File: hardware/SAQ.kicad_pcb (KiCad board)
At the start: 2 copper layers, 61 x 43.2 mm, 40 parts, among them J1 Sens, J2 9V, J3 AudioJack2_Ground_Switch, J4 SP, Q1 2N3904, SW1 SW_SPDT, U1 LM555, U2 LM386

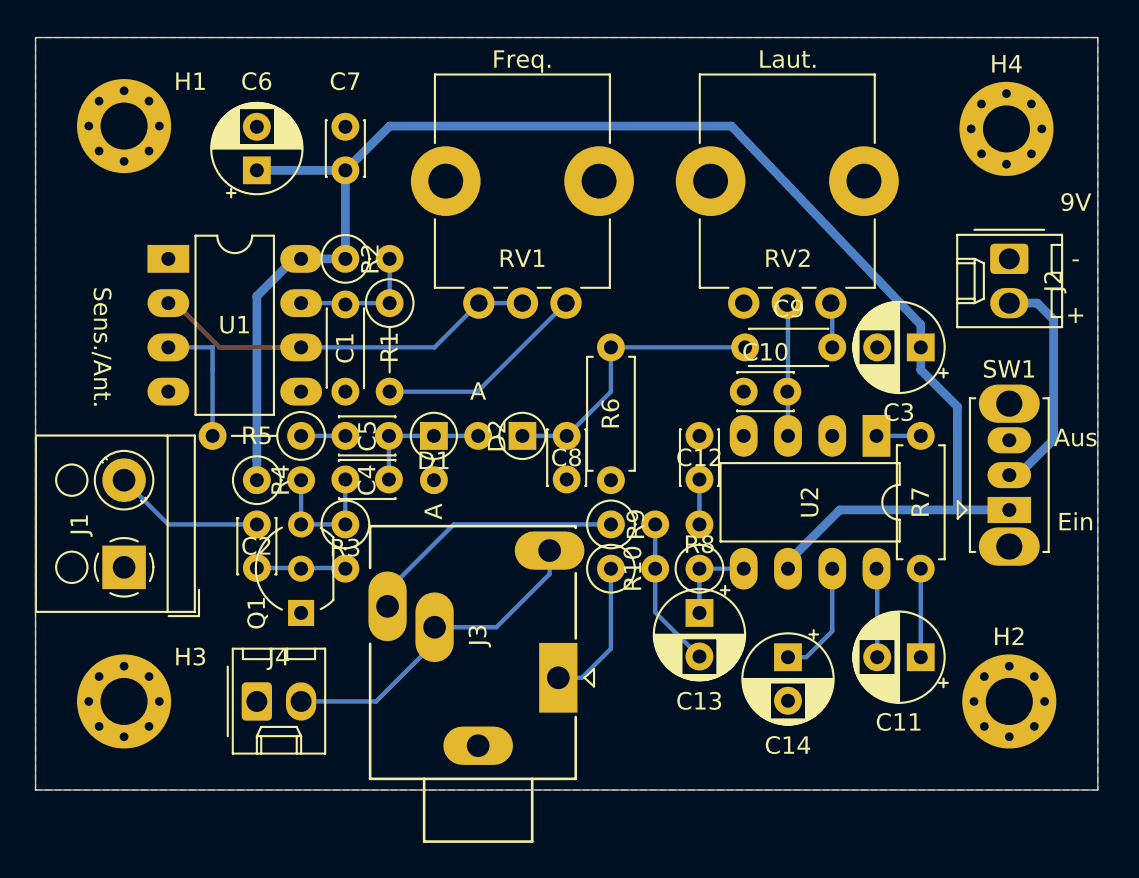
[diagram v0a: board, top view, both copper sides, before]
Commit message: Fixed LM555 circuit & Caps.
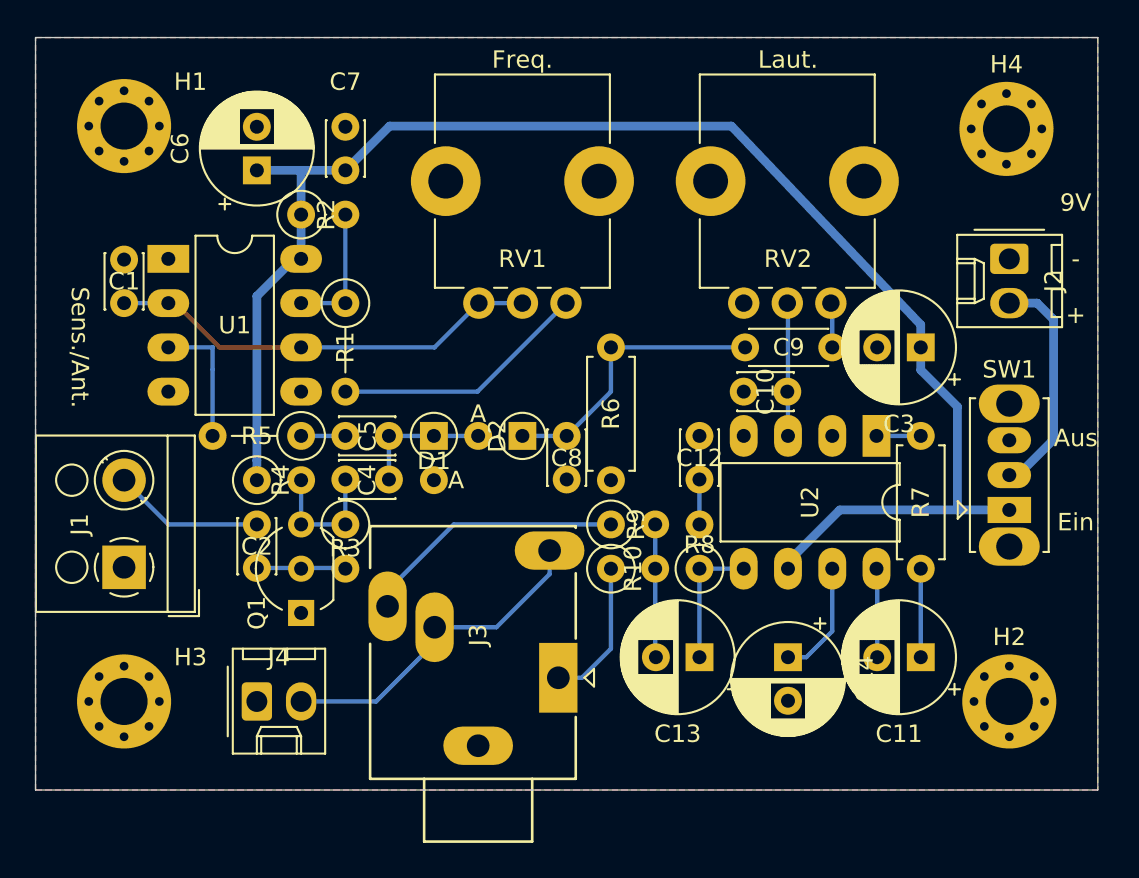
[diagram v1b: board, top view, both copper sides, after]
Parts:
- C1: value 680p -> 680p*; footprint Capacitor_THT:C_Disc_D4.3mm_W1.9mm_P5.00mm -> Capacitor_THT:C_Disc_D3.0mm_W2.0mm_P2.50mm
- C11, C13, C14, C3, C6: footprint Capacitor_THT:CP_Radial_D5.0mm_P2.50mm -> Capacitor_THT:CP_Radial_D6.3mm_P2.50mm
- J3: value AudioJack2_Ground_Switch -> out
- R2: value 39k -> 6.8k
- RV1: value 47k -> 100k
- moved C1 14.8 mm to (124.5, 92.8), turned to 270 degrees
- moved R2 3.59 mm to (134.6, 90.2)
- moved C13 2.54 mm to (157.5, 115.6), turned to 180 degrees
- moved R1 2.54 mm to (137.2, 95.2)
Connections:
- R1 pad 1: Net-(C1-Pad2) -> Net-(R1-Pad1)
- R2 pad 2: Net-(C1-Pad2) -> Net-(R1-Pad1)
- RV1 pad 2: Net-(RV1-Pad2) -> Net-(C1-Pad2)
- RV1 pad 3: Net-(RV1-Pad2) -> Net-(C1-Pad2)
- U1 pad 2: Net-(RV1-Pad2) -> Net-(C1-Pad2)
- U1 pad 6: Net-(RV1-Pad2) -> Net-(C1-Pad2)
- U1 pad 7: Net-(C1-Pad2) -> Net-(R1-Pad1)
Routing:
- net Net-(RV1-Pad2): track 22.4 -> 0.00 mm
- net Net-(C1-Pad2): track 7.62 -> 25.0 mm
- net Net-(R1-Pad1): track 0.00 -> 7.62 mm
- net VCC: track 91.5 -> 88.9 mm
- net Net-(R1-Pad2): track 12.2 -> 14.8 mm
- net Net-(C13-Pad1): track 5.08 -> 7.62 mm
- net Net-(C13-Pad2): track 8.63 -> 7.64 mm

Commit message: Fixed PCB.
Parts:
- C7: footprint Capacitor_THT:C_Disc_D3.0mm_W2.0mm_P2.50mm -> Capacitor_THT:C_Disc_D4.3mm_W1.9mm_P5.00mm
- H1, H2, H3, H4: footprint MountingHole:MountingHole_2.7mm_M2.5_Pad_Via -> MountingHole:MountingHole_3.2mm_M3_Pad_Via
- J1: value Sens -> Sense; footprint TerminalBlock_RND:TerminalBlock_RND_205-00001_1x02_P5.00mm_Horizontal -> TerminalBlock_RND:TerminalBlock_RND_205-00013_1x03_P5.00mm_Horizontal
- moved C7 26.4 mm to (129.5, 110.4), turned to 90 degrees
- moved C1 2.54 mm to (127.0, 92.8)
- moved R1 2.54 mm to (139.7, 95.2)
- moved R2 2.54 mm to (137.2, 90.2)
- moved U1 2.54 mm to (129.5, 92.7)
- moved C6 2.50 mm to (134.6, 87.6), turned to 180 degrees
- moved J1 0.08 mm to (124.5, 110.3)
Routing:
- net Net-(C2-Pad2): track 8.67 -> 13.7 mm
- net Net-(C1-Pad2): track 25.0 -> 22.4 mm
- net Net-(R1-Pad2): track 14.8 -> 12.2 mm
- net OSC: track 7.62 -> 8.78 mm
- net VCC: track 88.9 -> 90.0 mm

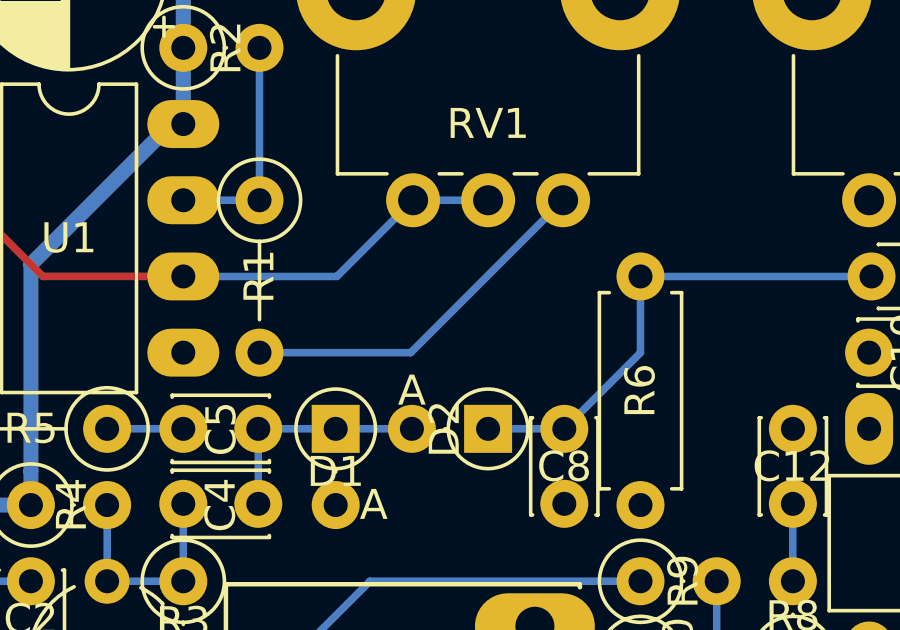
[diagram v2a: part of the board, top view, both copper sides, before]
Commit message: Added prototype circuit/board
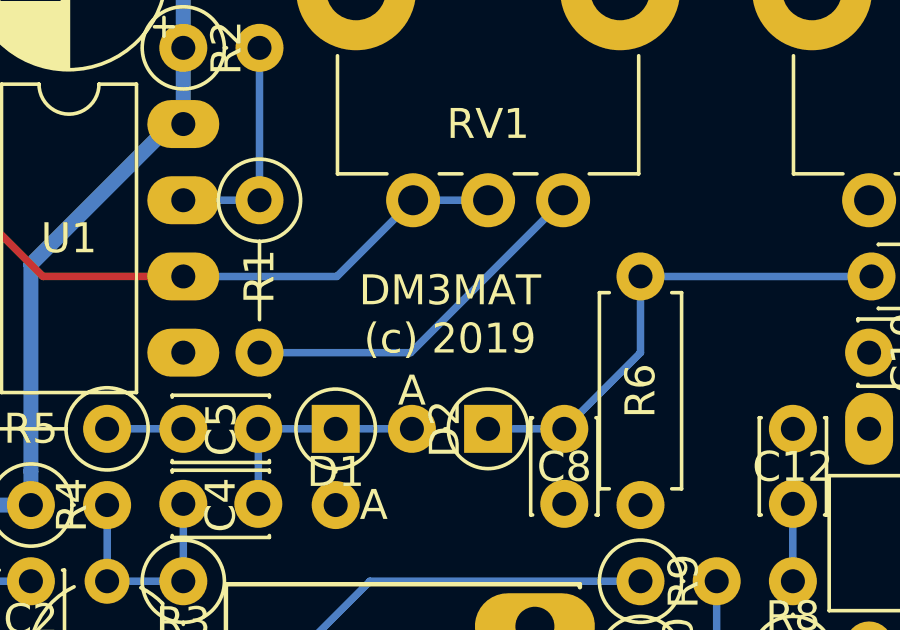
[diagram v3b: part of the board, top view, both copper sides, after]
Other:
- board text added: "DM3MAT (c) 2019"
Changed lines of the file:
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@@
   (general
     (thickness 1.6)
-    (drawings 11)
+    (drawings 12)
     (tracks 85)
     (zones 0)
@@
     )
   )
+  (gr_text "DM3MAT\n(c) 2019" (at 146.05 99.06) (layer F.SilkS)
+    (effects (font (size 1 1) (thickness 0.15)))
+  )
   (dimension 60.96 (width 0.15) (layer Dwgs.User)
